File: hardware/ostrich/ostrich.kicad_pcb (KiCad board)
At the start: 4 copper layers, 53.3 x 83.8 mm, 54 parts, among them J1 CONN_01X40, J2 CONN_01X08, J3 CONN_01X06, J4 CONN_01X10, J5 CONN_01X08, J6 CONN_01X10, J7 Micro_SD_Card_CD, J8 CONN_01X13, J9 CONN_01X04, M1 ESP-11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

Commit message: Fixed SD slot orientation and diode footprint
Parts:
- D1, D2: footprint Diodes_SMD:D_0805 -> Diodes_SMD:D_1206
- R10, R7, R8, R9: value 1KR -> 100R
- moved C16 14.0 mm to (100.6, 92.2), turned to 270 degrees
- moved J7 12.6 mm to (101.1, 75.4), turned to 270 degrees
- moved R1 5.11 mm to (104.6, 88.1), turned to 0 degrees
- moved Q1 2.44 mm to (105.4, 99.1)
- moved C6 1.52 mm to (142.5, 84.3)
- moved D2 1.09 mm to (141.7, 81.8)
- moved D1 0.76 mm to (106.7, 94.7)
- moved R2 0.63 mm to (103.6, 94.0)
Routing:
- net +3V3: track 138.1 -> 158.7 mm, vias 30 -> 32
- net /SD_MISO: track 19.1 -> 37.2 mm, vias 2 -> 4
- net /SD_SCLK: track 14.3 -> 29.2 mm, vias 2 -> 4
- net /SD_CS: track 20.3 -> 34.7 mm, vias 2 -> 4
- net GND: track 136.0 -> 148.8 mm, vias 43 -> 41
- net /SD_MOSI: track 23.3 -> 34.8 mm
- net /SD_CD: track 20.4 -> 27.7 mm, vias 2 -> 3
- net /Vusb: track 10.9 -> 6.66 mm
- net /NRST: track 96.0 -> 99.0 mm
- net Net-(D1-Pad2): track 59.9 -> 62.6 mm
- net VCC: track 113.6 -> 116.1 mm
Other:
- board text added: "Rev 2"
- board text removed: "Rev 1"

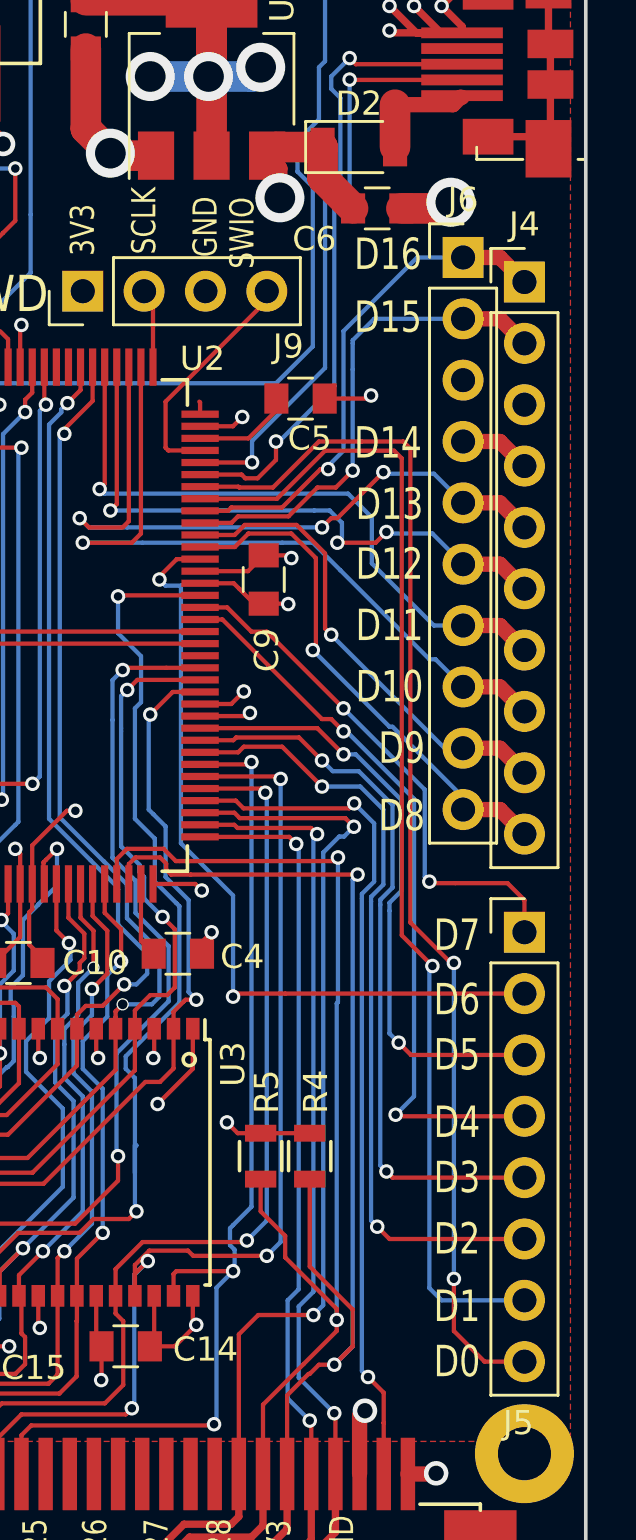
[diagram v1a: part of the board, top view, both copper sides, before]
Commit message: Added Vbus and rearranged digital pins
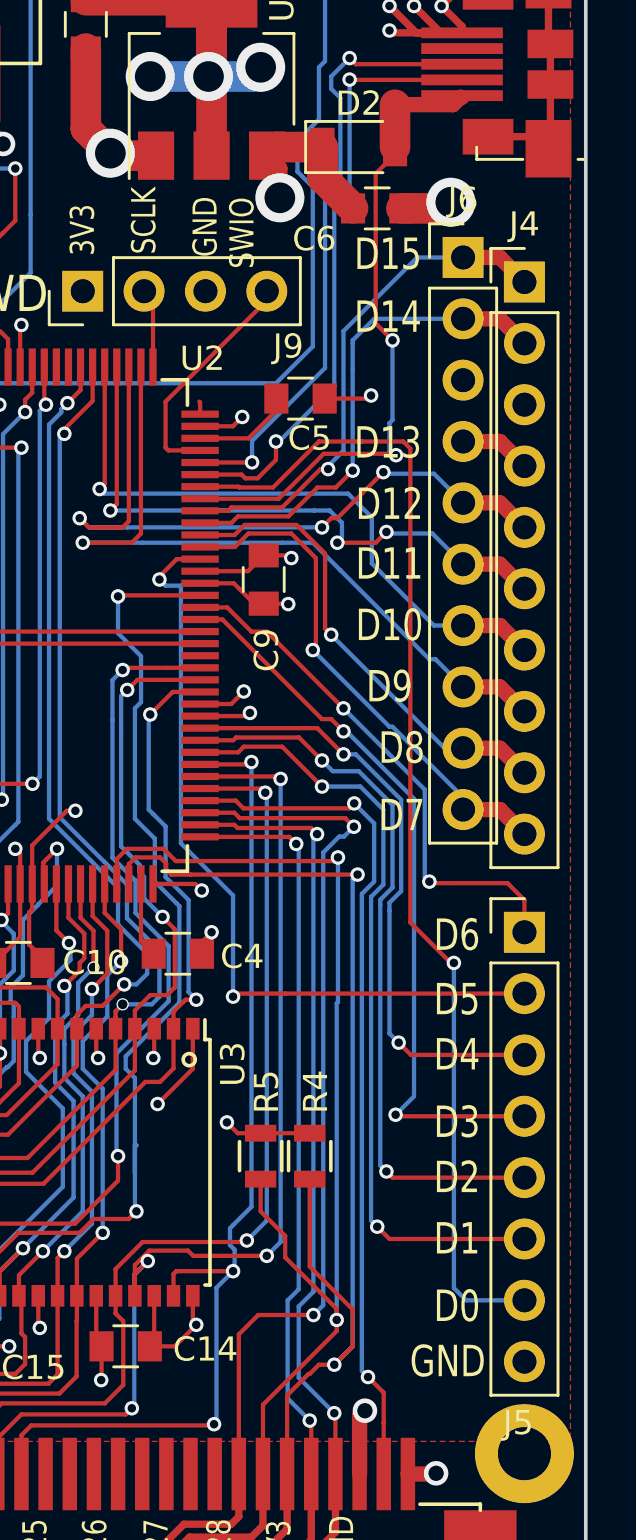
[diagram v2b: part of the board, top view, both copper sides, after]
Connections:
- net Net-(U2-Pad43) renamed /PA7
- D2 pad 2: /Vusb -> /PA9
- J5 pad 7: /PA9 -> /PA10
- J5 pad 8: /PA10 -> GND
- P1 pad 1: /Vusb -> /PA9
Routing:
- net /PA9: track 48.4 -> 28.6 mm, vias 1 -> 2
- net /Vusb: track 6.66 -> 0.00 mm
- net /PA10: track 50.4 -> 48.3 mm, vias 2 -> 1
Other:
- board text removed: "D16"

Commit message: Updated footprint table for KiCad 5, removed 0.1 inch aligned connector, and added all SWD pins
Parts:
- removed J6: CONN_01X10, Pin_Headers:Pin_Header_Straight_1x10_Pitch2.54mm
- J4: footprint Pin_Headers:Pin_Header_Straight_1x10_Pitch2.54mm -> Connector_PinHeader_2.54mm:PinHeader_1x10_P2.54mm_Vertical
- J9: value CONN_01X04 -> CONN_01X06; footprint Pin_Headers:Pin_Header_Straight_1x04_Pitch2.54mm -> Connector_PinHeader_2.54mm:PinHeader_1x06_P2.54mm_Vertical
- moved J9 0.18 mm to (130.2, 87.6)
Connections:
- U2 pad 133: Net-(U2-Pad133) -> /SWO
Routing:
- net /SWO: track 0.00 -> 29.1 mm, vias 0 -> 2
- net /USB_DM: track 25.3 -> 28.4 mm
- net /PC9: track 20.5 -> 17.5 mm
- net GND: track 148.8 -> 145.8 mm
- net /PA8: track 21.2 -> 18.8 mm
- net /PA9: track 28.6 -> 30.3 mm
- net +3V3: track 158.7 -> 159.8 mm, vias 32 -> 33
- net /NRST: track 99.0 -> 98.5 mm
- net /USB_DP: track 25.6 -> 26.2 mm
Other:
- board text removed: "SCLK"
- board text removed: "SWIO"
